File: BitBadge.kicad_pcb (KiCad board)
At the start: 2 copper layers, 64 x 67.1 mm, 72 parts, among them SW1 SW_2P3T

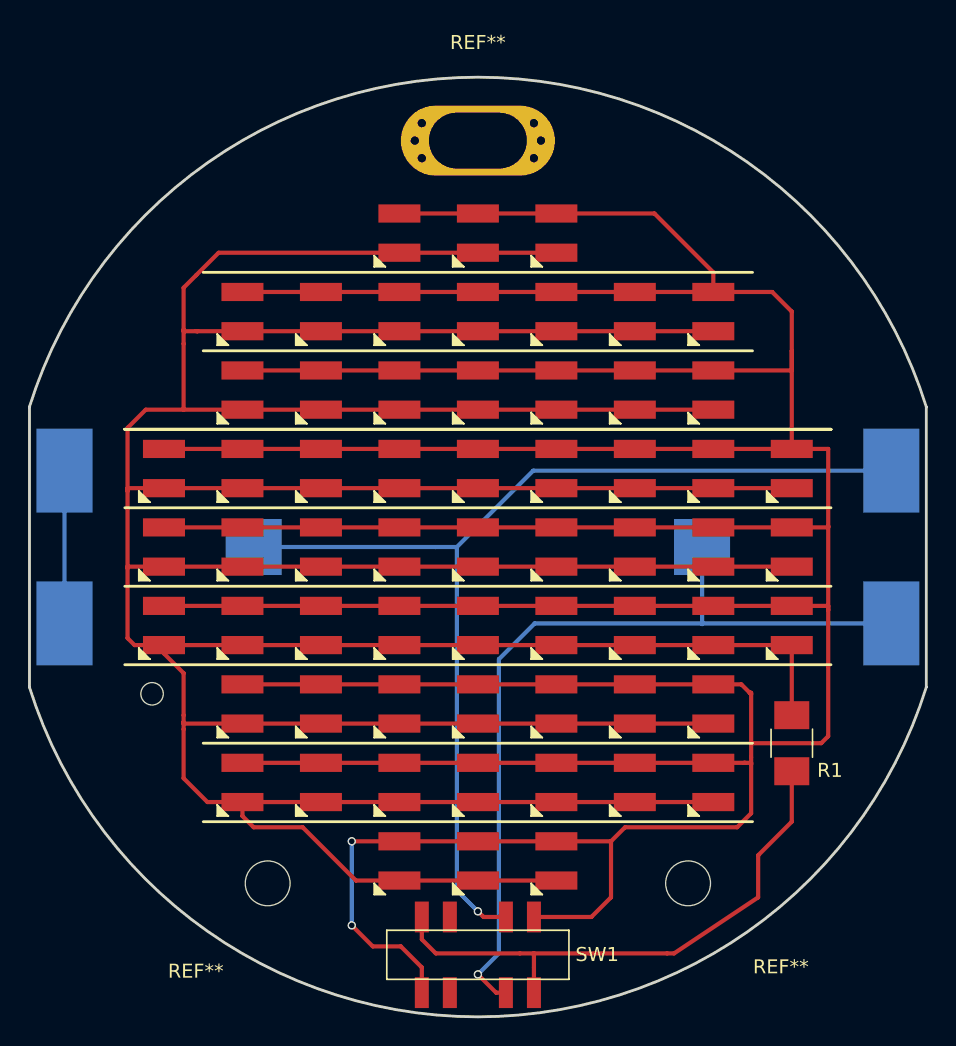
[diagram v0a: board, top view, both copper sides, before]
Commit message: New pads for Blinke-LEDs
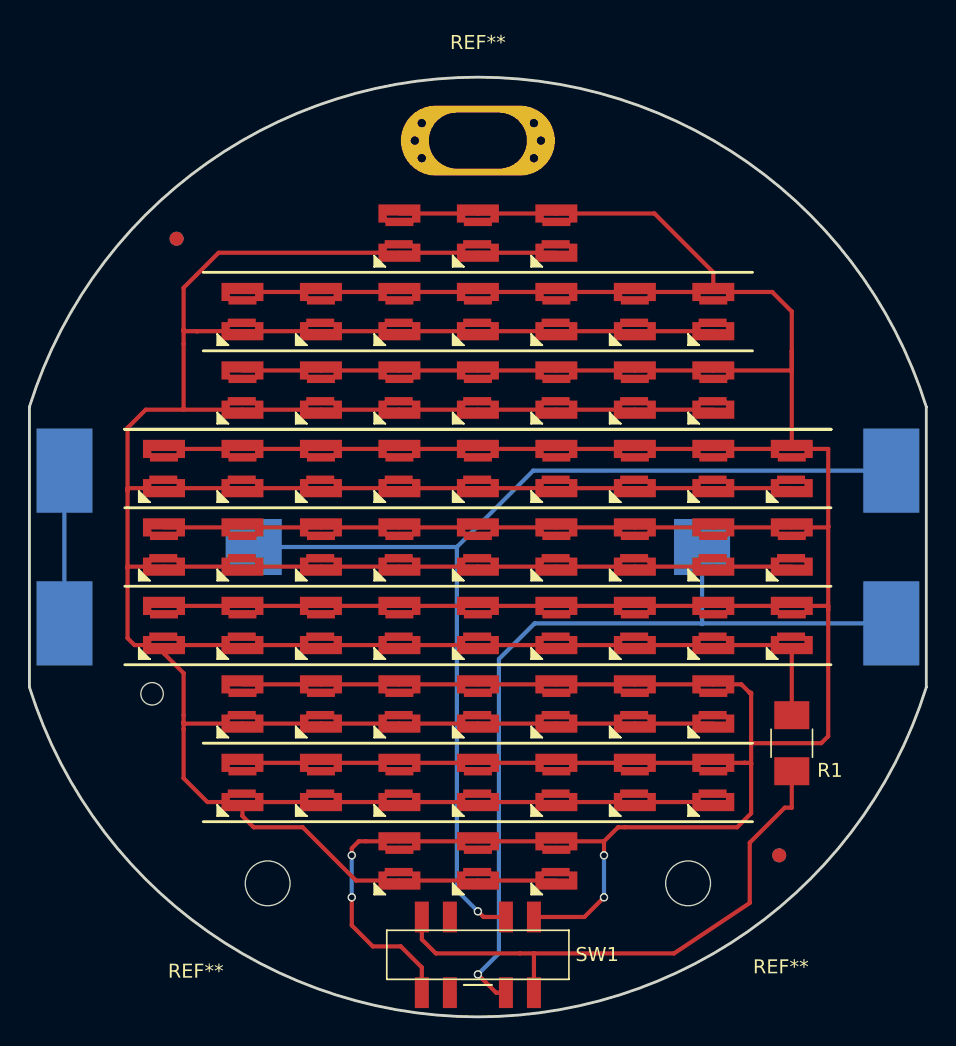
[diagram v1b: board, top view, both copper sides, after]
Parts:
- added FID1: Fiducial, GaudiLabsFootPrints:Fiducial_1mm_Dia_2.54mm_Outer_CopperBottom, B.Cu at (121.5, 122.0)
- added FID2: Fiducial, GaudiLabsFootPrints:Fiducial_1mm_Dia_2.54mm_Outer_CopperBottom, F.Cu at (78.5, 78.0)
- added FID3: Fiducial, GaudiLabsFootPrints:Fiducial_1mm_Dia_2.54mm_Outer_CopperBottom, B.Cu at (78.5, 78.0)
- added FID4: Fiducial, GaudiLabsFootPrints:Fiducial_1mm_Dia_2.54mm_Outer_CopperBottom, F.Cu at (121.5, 122.0)
- D1, D10, D11, D12, D13, D14, D15, D16, D17, D18, D19, D2, D20, D21, D22, D23, D24, D25, D26, D27, D28, D29, D3, D30, D31, D32, D33, D34, D35, D36, D37, D38, D39, D4, D40, D41, D42, D43, D44, D45, D46, D47, D48, D49, D5, D50, D51, D52, D53, D54, D55, D56, D57, D58, D59, D6, D60, D61, D7, D8, D9: footprint GaudiLabsFootPrints:TopLed_BitBadge -> GaudiLabsFootPrints:TopLed_BitBadge_blink
- moved G*** 2.09 mm to (118.0, 116.0)
- moved G*** 2.09 mm to (82.0, 116.0)
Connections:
- SW1 pad 2: Net-(SW1-Pad2) -> (no net)
- SW1 pad 6: Net-(SW1-Pad6) -> (no net)
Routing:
- net Net-(D1-Pad1): track 419.9 -> 419.1 mm, vias 2 -> 4
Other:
- net class Default removed
- board text added: "V1.2 2021"
- board text removed: "V1.0 2018"
